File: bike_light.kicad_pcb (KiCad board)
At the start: 2 copper layers, 25.4 x 25.4 mm, 193 parts, among them Q1 AON7611, Q2 AON7611, Q3 AON7611, Q4 DMN65D8L, Q5 DMN65D8L, Q6 DMN65D8L, Q7 DMN65D8L, Q8 DMN65D8L, Q9 DMN65D8L, U1 TEST_PT, U10 TEST_PT, U11 TEST_PT, U12 TEST_PT, U13 TEST_PT, U14 TEST_PT, U15 TEST_PT, U16 TEST_PT, U17 TEST_PT, U18 TEST_PT, U19 TEST_PT, U2 TEST_PT, U20 MCP6L02, U21 74LVC2G06, U22 TPS3700, U23 NC7WZ08, U24 74LVC2G06, U25 TPS3700, U26 NC7WZ08, U27 74LVC2G06, U28 TPS3700, U29 NC7WZ08, U3 TEST_PT, U30 MSP430G2203IPW28, U31 BH1620FVC, U32 MMA7660FC, U33 AT42QT1011, U34 TOUCHPAD, U35 AT42QT1011, U36 TOUCHPAD, U37 AT42QT1011, U38 TOUCHPAD, U39 TLC59108IPWR, U4 TEST_PT, U40 TLC59108IPWR, U41 TLC59108IPWR, U42 TPS62090, U43 LM3668, U44 CONN_JTAG_14_2_wire, U45 CP2110, U46 ESDR0502N, U47 CONN_USB, U48 BQ24190, U5 TEST_PT, U6 TEST_PT, U7 TEST_PT, U8 TEST_PT, U9 TEST_PT

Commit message: Never thought 0805 would seem big...
But about 80% of the space is consumed by the 0805 resistor and caps.
01005? XD
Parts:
- C17, C18, C19, C20, C21, C22, C23, C24, C3, D14, D15, D16, D24, D25, D26, D27, D28, D29, D36, R31, R32, R33, R37, R38, R39, R40, R41, R42, R43, R44, U30, U39, U40, U41, U42: moved to B.Cu
- moved BT2 469.2 mm to (344.9, 191.5)
- moved D3 430.7 mm to (309.1, 132.8), turned to 45 degrees
- moved D4 424.1 mm to (310.5, 136.9), turned to 135 degrees
- moved R10 403.7 mm to (297.4, 131.2)
- moved R8 400.9 mm to (300.9, 144.8)
- moved U25 392.0 mm to (301.1, 142.1)
- moved U26 388.8 mm to (301.2, 136.8)
- moved R11 386.0 mm to (299.3, 129.0), turned to 180 degrees
- moved R9 382.8 mm to (304.8, 143.3)
- moved Q2 377.3 mm to (304.5, 135.5)
- moved R7 371.0 mm to (299.3, 133.3), turned to 180 degrees
- moved U24 362.8 mm to (301.8, 131.8)
- moved C21 339.3 mm to (355.9, 110.2)
- moved R42 333.3 mm to (349.4, 105.8), turned to 270 degrees
- moved C23 329.2 mm to (356.5, 105.8), turned to 270 degrees
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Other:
- board text added: "Rear Signal Module"
- board text removed: "Battery Control Module"

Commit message: moving around parts in pcb
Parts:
- moved D5 303.9 mm to (308.7, 131.1), turned to 45 degrees
- moved D6 296.4 mm to (309.8, 139.6), turned to 135 degrees
- moved R12 279.5 mm to (300.9, 124.1)
- moved Q3 277.6 mm to (309.0, 135.9)
- moved R15 274.0 mm to (301.6, 130.2)
- moved R13 268.1 mm to (302.1, 138.0)
- moved U28 266.0 mm to (305.2, 135.5)
- moved R16 254.4 mm to (300.7, 144.9)
- moved U27 247.5 mm to (301.4, 134.7)
- moved R14 239.9 mm to (299.5, 126.9)
- moved U29 235.6 mm to (301.8, 142.0), turned to 90 degrees
- moved BT3 235.4 mm to (231.0, 134.9)
- moved Q1 187.9 mm to (307.3, 77.0), turned to 180 degrees
- moved D2 165.1 mm to (308.6, 75.3), turned to 45 degrees
- moved D1 159.3 mm to (310.0, 82.8), turned to 135 degrees
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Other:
- board text added: "Front Signal Module"
- board text removed: "Rear Module"

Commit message: revisions to board and sch
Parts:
- removed BT2, BT3: BATTERY, BATT_18650
- removed D32: LY-E63F, LED_TOPLED_PWR
- removed D33, D34: LY-A67F, LED_SIDELED_PWR
- removed D35: LR-A67F, LED_SIDELED_PWR
- removed Q2, Q3: AON7611, DFN_3x3A_8L_EP1_P
- removed R13, R14: Nominal, r_0805
- removed R15: 102K, r_0805
- removed R16: 191K, r_0805
- removed R31, R32, R33, R34, R35, R36: 200, r_0805
- removed U24, U27: 74LVC2G06, SOT363
- removed U25, U28: TPS3700, SOT23_6_thin
- removed U26, U29: NC7WZ08, US8
- added P1: CONN_6_RA_MALE, CONN_3x2_MALE_RA, B.Cu at (461.0, 196.8)
- added P2: CONN_6_RA_FEMALE, CONN_3x2_FEMALE_RA, B.Cu at (335.3, 201.9)
- added P3: CONN_6_RA_MALE, CONN_3x2_MALE_RA, B.Cu at (344.2, 201.9)
- added P4: CONN_6_RA_MALE, CONN_3x2_MALE_RA, B.Cu at (313.7, 201.9)
- added P5: CONN_6_MALE_FRONT, CONN_3x2_FEMALE, B.Cu at (358.1, 201.9)
- added P6: CONN_6_MALE_BACK, CONN_3x2_FEMALE, B.Cu at (447.0, 196.8)
- BT1: moved to B.Cu
- D10: value LS-E63F -> LY-A67F; footprint LED_TOPLED_PWR -> LED_SIDELED_PWR; moved to B.Cu
- D11, D12, D13, D23: value LS-E63F -> LY-E63F
- D15, D16, D17, D18, D19: value LY-E63F -> LS-E63F
- D21, D22: value LS-E63F -> LR-A67F; footprint LED_TOPLED_PWR -> LED_SIDELED_PWR
- D26: value LY-E63F -> LY-A67F; footprint LED_TOPLED_PWR -> LED_SIDELED_PWR
- D28: value LY-A67F -> LY-E63F; footprint LED_SIDELED_PWR -> LED_TOPLED_PWR
- D29: value LR-A67F -> LY-E63F; footprint LED_SIDELED_PWR -> LED_TOPLED_PWR
- D3, D4, D5: value MBR1045ULPS -> LY-E63F; footprint TO_277B -> LED_TOPLED_PWR
- D6: value MBR1045ULPS -> LY-A67F; footprint TO_277B -> LED_SIDELED_PWR; moved to B.Cu
- R10: value 102K -> 200
- R11: value 191K -> 200
- R12, R7: value 1.58M -> 200
- R8, R9: value Nominal -> 200
- moved U20 550.8 mm to (388.6, 203.2)
- moved C2 549.8 mm to (387.4, 208.3)
- moved C1 543.4 mm to (387.4, 198.1)
- moved U11 513.3 mm to (401.3, 185.4)
- moved U14 513.3 mm to (381.0, 185.4)
- moved U17 513.3 mm to (426.7, 185.4)
- moved U18 513.3 mm to (419.1, 185.4)
- moved U2 513.3 mm to (388.6, 185.4)
- moved U3 513.3 mm to (439.4, 185.4)
- moved U6 513.3 mm to (408.9, 185.4)
- moved U8 513.3 mm to (368.3, 185.4)
- moved U1 513.3 mm to (386.1, 185.4)
- moved U10 513.3 mm to (398.8, 185.4)
- moved U12 513.3 mm to (393.7, 185.4)
- moved U13 513.3 mm to (406.4, 185.4)
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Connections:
- C22 pad 1: /output_signal_brake_2/+2.5V local -> /output_signal_brake_2/brake_leds/+2.5V
- D10 pad 1: /output_signal_brake_2/+2.5V local -> /output_signal_brake_2/brake_leds/+2.5V
- D10 pad 2: /output_signal_brake_2/+2.5V local -> /output_signal_brake_2/signal_leds_front/CATHODE_8
- D11 pad 1: /output_signal_brake_2/+2.5V local -> /output_signal_brake_2/brake_leds/+2.5V
- D11 pad 2: /output_signal_brake_2/+2.5V local -> /output_signal_brake_2/brake_leds/+2.5V
- D11 pad 3: /output_signal_brake_2/+2.5V local -> /output_signal_brake_2/brake_leds/+2.5V
- D11 pad 4: N-00000146 -> /output_signal_brake_2/signal_leds_front/CATHODE_1
- D12 pad 1: /output_signal_brake_2/+2.5V local -> /output_signal_brake_2/brake_leds/+2.5V
- D12 pad 2: /output_signal_brake_2/+2.5V local -> /output_signal_brake_2/brake_leds/+2.5V
- D12 pad 3: /output_signal_brake_2/+2.5V local -> /output_signal_brake_2/brake_leds/+2.5V
- D12 pad 4: N-00000167 -> /output_signal_brake_2/signal_leds_front/CATHODE_3
- D13 pad 1: /output_signal_brake_2/+2.5V local -> /output_signal_brake_2/brake_leds/+2.5V
- D13 pad 2: /output_signal_brake_2/+2.5V local -> /output_signal_brake_2/brake_leds/+2.5V
- D13 pad 3: /output_signal_brake_2/+2.5V local -> /output_signal_brake_2/brake_leds/+2.5V
- D13 pad 4: N-00000147 -> /output_signal_brake_2/signal_leds_front/CATHODE_5
- D14 pad 1: /output_signal_brake_2/+2.5V local -> /output_signal_brake_2/brake_leds/+2.5V
- D14 pad 2: /output_signal_brake_2/+2.5V local -> /output_signal_brake_2/brake_leds/+2.5V
- D14 pad 3: /output_signal_brake_2/+2.5V local -> /output_signal_brake_2/brake_leds/+2.5V
- D14 pad 4: N-00000112 (its old number) -> /output_signal_brake_2/signal_leds_front/CATHODE_7
- D15 pad 1: /output_signal_brake_2/+2.5V local -> /output_signal_brake_2/brake_leds/+2.5V
- D15 pad 2: /output_signal_brake_2/+2.5V local -> /output_signal_brake_2/brake_leds/+2.5V
- D15 pad 3: /output_signal_brake_2/+2.5V local -> /output_signal_brake_2/brake_leds/+2.5V
- D15 pad 4: N-00000113 -> /output_signal_brake_2/brake_leds/CATHODE_2
- D16 pad 1: /output_signal_brake_2/+2.5V local -> /output_signal_brake_2/brake_leds/+2.5V
- D16 pad 2: /output_signal_brake_2/+2.5V local -> /output_signal_brake_2/brake_leds/+2.5V
- D16 pad 3: /output_signal_brake_2/+2.5V local -> /output_signal_brake_2/brake_leds/+2.5V
- D16 pad 4: N-00000114 -> /output_signal_brake_2/brake_leds/CATHODE_4
- D17 pad 1: /output_signal_brake_2/+2.5V local -> /output_signal_brake_2/brake_leds/+2.5V
- D17 pad 2: /output_signal_brake_2/+2.5V local -> /output_signal_brake_2/brake_leds/+2.5V
- D17 pad 3: /output_signal_brake_2/+2.5V local -> /output_signal_brake_2/brake_leds/+2.5V
- D17 pad 4: N-00000140 -> /output_signal_brake_2/brake_leds/CATHODE_6
- D18 pad 1: /output_signal_brake_2/+2.5V local -> /output_signal_brake_2/brake_leds/+2.5V
- D18 pad 2: /output_signal_brake_2/+2.5V local -> /output_signal_brake_2/brake_leds/+2.5V
- D18 pad 3: /output_signal_brake_2/+2.5V local -> /output_signal_brake_2/brake_leds/+2.5V
- D18 pad 4: N-00000142 -> /output_signal_brake_2/brake_leds/CATHODE_1
- D19 pad 1: /output_signal_brake_2/+2.5V local -> /output_signal_brake_2/brake_leds/+2.5V
- D19 pad 2: /output_signal_brake_2/+2.5V local -> /output_signal_brake_2/brake_leds/+2.5V
- D19 pad 3: /output_signal_brake_2/+2.5V local -> /output_signal_brake_2/brake_leds/+2.5V
- D19 pad 4: N-00000164 (its old number) -> /output_signal_brake_2/brake_leds/CATHODE_3
- D20 pad 1: /output_signal_brake_2/+2.5V local -> /output_signal_brake_2/brake_leds/+2.5V
- D20 pad 2: /output_signal_brake_2/+2.5V local -> /output_signal_brake_2/brake_leds/+2.5V
- D20 pad 3: /output_signal_brake_2/+2.5V local -> /output_signal_brake_2/brake_leds/+2.5V
- D20 pad 4: N-00000168 -> /output_signal_brake_2/brake_leds/CATHODE_5
- D21 pad 1: /output_signal_brake_2/+2.5V local -> /output_signal_brake_2/brake_leds/+2.5V
- D21 pad 2: /output_signal_brake_2/+2.5V local -> /output_signal_brake_2/brake_leds/CATHODE_7
- D22 pad 1: /output_signal_brake_2/+2.5V local -> /output_signal_brake_2/brake_leds/+2.5V
- D22 pad 2: /output_signal_brake_2/+2.5V local -> /output_signal_brake_2/brake_leds/CATHODE_8
- D23 pad 1: /output_signal_brake_2/+2.5V local -> /output_signal_brake_2/brake_leds/+2.5V
- D23 pad 2: /output_signal_brake_2/+2.5V local -> /output_signal_brake_2/brake_leds/+2.5V
- D23 pad 3: /output_signal_brake_2/+2.5V local -> /output_signal_brake_2/brake_leds/+2.5V
- D23 pad 4: N-00000165 -> /output_signal_brake_2/signal_leds_back/CATHODE_2
- D24 pad 1: /output_signal_brake_2/+2.5V local -> /output_signal_brake_2/brake_leds/+2.5V
- D24 pad 2: /output_signal_brake_2/+2.5V local -> /output_signal_brake_2/brake_leds/+2.5V
- D24 pad 3: /output_signal_brake_2/+2.5V local -> /output_signal_brake_2/brake_leds/+2.5V
- D24 pad 4: N-00000109 -> /output_signal_brake_2/signal_leds_back/CATHODE_4
- D25 pad 1: /output_signal_brake_2/+2.5V local -> /output_signal_brake_2/brake_leds/+2.5V
- D25 pad 2: /output_signal_brake_2/+2.5V local -> /output_signal_brake_2/brake_leds/+2.5V
- D25 pad 3: /output_signal_brake_2/+2.5V local -> /output_signal_brake_2/brake_leds/+2.5V
- D25 pad 4: N-00000110 (its old number) -> /output_signal_brake_2/signal_leds_back/CATHODE_6
- D26 pad 1: /output_signal_brake_2/+2.5V local -> /output_signal_brake_2/brake_leds/+2.5V
- D26 pad 2: /output_signal_brake_2/+2.5V local -> /output_signal_brake_2/signal_leds_back/CATHODE_8
- D27 pad 1: /output_signal_brake_2/+2.5V local -> /output_signal_brake_2/brake_leds/+2.5V
- D27 pad 2: N-00000170 -> /output_signal_brake_2/signal_leds_back/CATHODE_8
- D28 pad 1: /output_signal_brake_2/+2.5V local -> /output_signal_brake_2/brake_leds/+2.5V
- D28 pad 2: N-00000170 -> /output_signal_brake_2/brake_leds/+2.5V
- D29 pad 1: /output_signal_brake_2/+2.5V local -> /output_signal_brake_2/brake_leds/+2.5V
- D29 pad 2: N-00000169 -> /output_signal_brake_2/brake_leds/+2.5V
- D3 pad 1: N-00000193 -> /output_signal_brake_2/brake_leds/+2.5V
- D3 pad 2: N-00000193 -> /output_signal_brake_2/brake_leds/+2.5V
- D3 pad 3: N-00000198 -> /output_signal_brake_2/brake_leds/+2.5V
- D30 pad 1: /output_signal_brake_2/+2.5V local -> /output_signal_brake_2/brake_leds/+2.5V
- D30 pad 2: /output_signal_brake_2/+2.5V local -> /output_signal_brake_2/brake_leds/+2.5V
- D30 pad 3: /output_signal_brake_2/+2.5V local -> /output_signal_brake_2/brake_leds/+2.5V
- D30 pad 4: N-00000144 -> /output_signal_brake_2/signal_leds_back/CATHODE_5
- D31 pad 1: /output_signal_brake_2/+2.5V local -> /output_signal_brake_2/brake_leds/+2.5V
- D31 pad 2: /output_signal_brake_2/+2.5V local -> /output_signal_brake_2/brake_leds/+2.5V
- D31 pad 3: /output_signal_brake_2/+2.5V local -> /output_signal_brake_2/brake_leds/+2.5V
- D31 pad 4: N-00000141 -> /output_signal_brake_2/signal_leds_back/CATHODE_7
- D4 pad 1: N-00000199 -> /output_signal_brake_2/brake_leds/+2.5V
- D4 pad 2: N-00000199 -> /output_signal_brake_2/brake_leds/+2.5V
- D4 pad 3: N-00000193 -> /output_signal_brake_2/brake_leds/+2.5V
- D5 pad 1: N-00000212 -> /output_signal_brake_2/brake_leds/+2.5V
- D5 pad 2: N-00000212 -> /output_signal_brake_2/brake_leds/+2.5V
- D5 pad 3: N-00000208 -> /output_signal_brake_2/brake_leds/+2.5V
- D6 pad 1: N-00000211 -> /output_signal_brake_2/brake_leds/+2.5V
- D6 pad 2: N-00000211 -> /output_signal_brake_2/signal_leds_front/CATHODE_8
- R10 pad 1: N-00000200 -> /output_signal_brake_2/brake_leds/+2.5V
- R10 pad 2: N-00000202 -> /output_signal_brake_2/brake_leds/CATHODE_8
- R11 pad 1: N-00000202 -> /output_signal_brake_2/brake_leds/+2.5V
- R11 pad 2: AGND -> /output_signal_brake_2/brake_leds/CATHODE_8
- R12 pad 1: N-00000212 -> /output_signal_brake_2/brake_leds/+2.5V
- R12 pad 2: N-00000205 -> /output_signal_brake_2/signal_leds_back/CATHODE_8
- R42 pad 1: /output_signal_brake_2/+2.5V local -> /output_signal_brake_2/brake_leds/+2.5V
- R43 pad 1: /output_signal_brake_2/+2.5V local -> /output_signal_brake_2/brake_leds/+2.5V
- R7 pad 1: N-00000193 -> /output_signal_brake_2/brake_leds/+2.5V
- R7 pad 2: N-00000200 -> /output_signal_brake_2/signal_leds_front/CATHODE_8
- R8 pad 1: +3.3V -> /output_signal_brake_2/brake_leds/+2.5V
- R8 pad 2: /battery_pack/battery_module_2/~UV -> /output_signal_brake_2/brake_leds/CATHODE_7
- R9 pad 1: +3.3V -> /output_signal_brake_2/brake_leds/+2.5V
- R9 pad 2: /battery_pack/battery_module_2/~OV -> /output_signal_brake_2/brake_leds/CATHODE_7
- U39 pad 10: N-00000146 -> /output_signal_brake_2/signal_leds_front/CATHODE_4
- U39 pad 11: N-00000148 -> /output_signal_brake_2/signal_leds_front/CATHODE_5
- U39 pad 12: N-00000167 -> /output_signal_brake_2/signal_leds_front/CATHODE_6
- U39 pad 14: N-00000165 -> /output_signal_brake_2/signal_leds_front/CATHODE_7
- U39 pad 15: N-00000147 -> /output_signal_brake_2/signal_leds_front/CATHODE_8
- U39 pad 6: N-00000168 -> /output_signal_brake_2/signal_leds_front/CATHODE_1
- U39 pad 7: N-00000145 -> /output_signal_brake_2/signal_leds_front/CATHODE_2
- U39 pad 9: N-00000166 -> /output_signal_brake_2/signal_leds_front/CATHODE_3
- U40 pad 10: N-00000113 -> /output_signal_brake_2/signal_leds_back/CATHODE_4
- U40 pad 11: N-00000111 -> /output_signal_brake_2/signal_leds_back/CATHODE_5
- U40 pad 12: N-00000114 -> /output_signal_brake_2/signal_leds_back/CATHODE_6
- U40 pad 14: N-00000170 -> /output_signal_brake_2/signal_leds_back/CATHODE_7
- U40 pad 15: N-00000169 -> /output_signal_brake_2/signal_leds_back/CATHODE_8
- U40 pad 6: N-00000109 -> /output_signal_brake_2/signal_leds_back/CATHODE_1
- U40 pad 7: N-00000112 (its old number) -> /output_signal_brake_2/signal_leds_back/CATHODE_2
- U40 pad 9: N-00000110 (its old number) -> /output_signal_brake_2/signal_leds_back/CATHODE_3
- U41 pad 10: N-00000142 -> /output_signal_brake_2/brake_leds/CATHODE_4
- U41 pad 11: N-00000143 -> /output_signal_brake_2/brake_leds/CATHODE_5
- U41 pad 12: N-00000164 (its old number) -> /output_signal_brake_2/brake_leds/CATHODE_6
- U41 pad 14: N-00000163 (its old number) -> /output_signal_brake_2/brake_leds/CATHODE_7
- U41 pad 15: N-00000139 -> /output_signal_brake_2/brake_leds/CATHODE_8
- U41 pad 6: N-00000144 -> /output_signal_brake_2/brake_leds/CATHODE_1
- U41 pad 7: N-00000140 -> /output_signal_brake_2/brake_leds/CATHODE_2
- U41 pad 9: N-00000141 -> /output_signal_brake_2/brake_leds/CATHODE_3
- U42 pad 16: /output_signal_brake_2/+2.5V local -> /output_signal_brake_2/brake_leds/+2.5V
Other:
- board outline removed

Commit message: revised layout considerably. more compact
almost ready for routing
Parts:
- C20, C21, C22, C23, C24, C3, D15, D16, D24, D25, D28, D29, D36, R40, R41, R42, R43, R44, U30, U42: moved to F.Cu
- D21, D22, D31, R10, R11, R12, R7, R8, R9: moved to B.Cu
- moved R7 188.5 mm to (468.6, 194.3)
- moved C29 174.6 mm to (432.6, 193.8)
- moved R46 173.1 mm to (432.6, 196.1)
- moved U44 172.3 mm to (411.0, 193.5)
- moved U40 170.2 mm to (306.1, 199.4)
- moved C17 168.0 mm to (306.1, 205.7), turned to 180 degrees
- moved R38 167.7 mm to (306.1, 208.3), turned to 180 degrees
- moved R47 162.4 mm to (396.0, 197.1)
- moved C30 158.3 mm to (396.5, 194.8)
- moved R37 157.5 mm to (468.6, 205.7)
- moved U45 157.1 mm to (401.1, 200.2), turned to 270 degrees
- moved C27 156.8 mm to (432.6, 189.2)
- moved C28 154.3 mm to (432.6, 191.5)
- moved U46 154.1 mm to (401.1, 195.8), turned to 90 degrees
- moved C19 153.2 mm to (466.1, 205.7)
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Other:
- board text added: "Back Signal"
- board text added: "Brake"
- board text added: "Touch Adj +"
- board text added: "Touch Adj -"
- board text added: "Touch Main"
- board text removed: "Battery Module"
- board text removed: "Battery modules"
- board text removed: "Front Signal Module"
- board text removed: "Interaction Module"
- board text removed: "Interface Module"
- board text removed: "Rear Signal Module"
- board text removed: "Sensor Module"

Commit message: replacement of parts, moved parts, preparing for routing
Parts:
- added L1: 1uH, smt_1816, F.Cu at (388.5, 189.4)
- added L2: 2.2uH, smt_1008, F.Cu at (400.8, 205.7)
- added L3: 2.2uH, smt_1816, F.Cu at (389.9, 198.5)
- added R1: R, r_0805, F.Cu at (386.3, 209.8)
- added TH1: NTC 10K, r_0402, F.Cu at (367.4, 201.8)
- added TH2: NTC 10K, r_0402, F.Cu at (376.9, 196.1)
- C1, C10, C11, C12, C13, C14, C15, C16, C17, C18, C19, C2, C20, C21, C22, C23, C24, C25, C26, C27, C28, C29, C3, C30, C31, C32, C33, C34, C35, C36, C37, C4, C5, C6, C7, C8, C9, R10, R11, R12, R17, R18, R19, R2, R20, R21, R22, R23, R24, R25, R26, R27, R28, R29, R3, R30, R37, R38, R39, R4, R40, R41, R42, R43, R44, R45, R46, R47, R48, R49, R5, R50, R51, R52, R53, R54, R55, R56, R57, R58, R6, R7, R8, R9: footprint r_0805 -> r_0603
- P1, P3, P4: footprint CONN_3x2_MALE_RA -> CONN_6_MALE_RA
- P2: footprint CONN_3x2_FEMALE_RA -> CONN_6_FEMALE
- P5, P6: footprint CONN_3x2_FEMALE -> CONN_6_FEMALE
- U43: footprint bnc -> WSON_12
- moved U43 74.0 mm to (404.5, 206.8), turned to 270 degrees
- moved R57 27.7 mm to (367.0, 203.2)
- moved U23 19.6 mm to (374.3, 189.6), turned to 180 degrees
- moved U21 17.7 mm to (376.4, 190.9), turned to 180 degrees
- moved R7 16.6 mm to (461.0, 209.0), turned to 90 degrees
- moved Q1 15.4 mm to (369.6, 192.5), turned to 0 degrees
- moved R58 14.9 mm to (377.1, 197.6)
- moved R6 14.0 mm to (361.9, 203.2), turned to 270 degrees
- moved U48 13.7 mm to (395.4, 195.8), turned to 90 degrees
- moved R40 13.5 mm to (360.2, 195.7), turned to 180 degrees
- moved C20 12.5 mm to (360.2, 197.4), turned to 180 degrees
- moved C3 12.3 mm to (426.0, 209.6), turned to 180 degrees
- moved R5 12.2 mm to (361.9, 200.4), turned to 270 degrees
- moved R37 11.9 mm to (463.8, 194.8), turned to 0 degrees
- moved D1 11.6 mm to (361.9, 194.1)
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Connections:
- R41 pad 1: (no net) -> /output_signal_brake_2/brake_leds/+2.5V
- R41 pad 2: (no net) -> N-00000163
- R44 pad 1: (no net) -> N-00000163
- R44 pad 2: (no net) -> AGND

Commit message: organizing parts...
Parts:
- moved L2 293.4 mm to (146.2, 60.1)
- moved R45 293.1 mm to (153.3, 63.4)
- moved C25 293.1 mm to (147.1, 63.8)
- moved D37 293.1 mm to (150.7, 64.0)
- moved U43 293.1 mm to (150.0, 61.3)
- moved C26 293.0 mm to (153.3, 60.6)
- moved R1 290.7 mm to (127.1, 78.1)
- moved U48 286.5 mm to (134.1, 78.1), turned to 135 degrees
- moved R54 283.5 mm to (134.1, 74.3), turned to 90 degrees
- moved U20 281.5 mm to (127.5, 74.0), turned to 90 degrees
- moved L3 281.2 mm to (133.1, 83.8), turned to 180 degrees
- moved C21 280.7 mm to (137.4, 66.5)
- moved C22 280.7 mm to (135.8, 61.1)
- moved C23 280.7 mm to (131.3, 63.8)
- moved C24 280.7 mm to (132.6, 66.7)
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
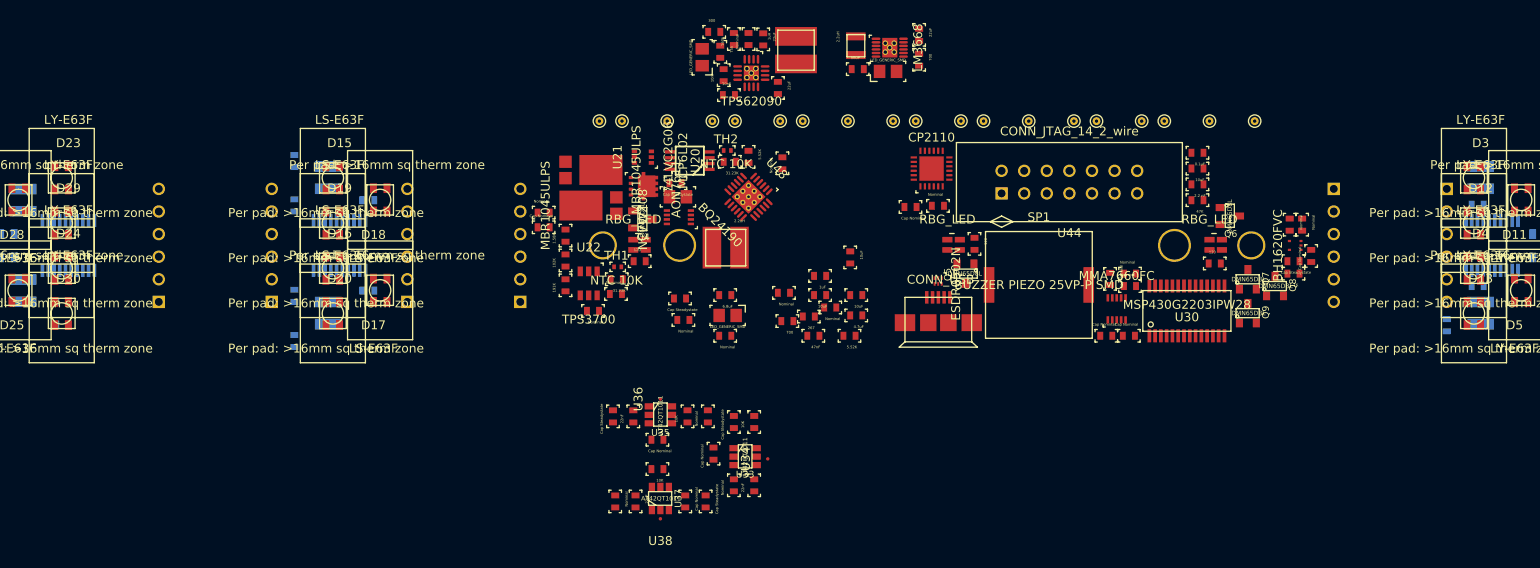
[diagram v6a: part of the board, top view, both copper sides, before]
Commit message: rearranged components, revised footprints
also planned power/gnd planes. haven't routed anything yet
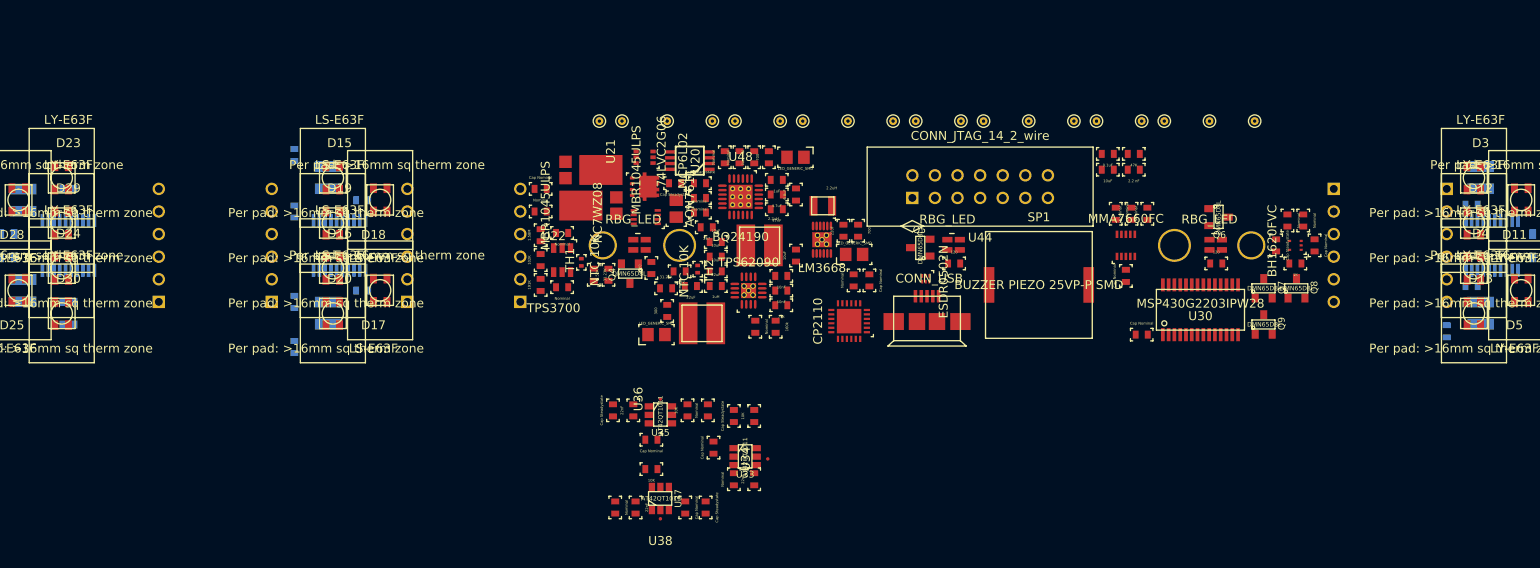
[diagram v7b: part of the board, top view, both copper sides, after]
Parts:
- moved L1 33.5 mm to (130.4, 92.3), turned to 180 degrees
- moved R41 33.4 mm to (137.2, 92.7), turned to 90 degrees
- moved R43 33.0 mm to (134.9, 92.7), turned to 90 degrees
- moved D36 32.4 mm to (124.7, 93.6), turned to 180 degrees
- moved R42 31.9 mm to (125.0, 90.9), turned to 270 degrees
- moved R44 28.6 mm to (137.8, 90.3), turned to 0 degrees
- moved C22 28.2 mm to (127.6, 88.1), turned to 0 degrees
- moved R53 27.3 mm to (118.4, 86.9), turned to 270 degrees
- moved C23 25.7 mm to (137.8, 88.6), turned to 0 degrees
- moved U42 24.4 mm to (134.1, 88.6), turned to 0 degrees
- moved C26 23.0 mm to (144.8, 81.9), turned to 270 degrees
- moved U43 22.9 mm to (142.4, 82.9), turned to 180 degrees
- moved C21 22.7 mm to (130.4, 88.1), turned to 180 degrees
- moved C25 22.3 mm to (139.4, 84.7), turned to 270 degrees
- moved C24 21.0 mm to (137.8, 87.0), turned to 0 degrees
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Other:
- board text added: "Front"

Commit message: parts arranged plausibly
maybe ready for routing?
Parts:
- moved P2 88.9 mm to (157.9, 46.1)
- moved P4 88.7 mm to (144.8, 45.8)
- moved R38 27.9 mm to (82.0, 79.0), turned to 0 degrees
- moved U40 26.3 mm to (83.9, 83.6)
- moved D26 25.9 mm to (78.5, 87.4)
- moved D27 25.9 mm to (78.5, 79.6)
- moved D25 25.6 mm to (76.8, 88.1)
- moved D28 25.5 mm to (76.8, 79.0)
- moved C17 24.4 mm to (82.0, 88.3), turned to 0 degrees
- moved D31 24.0 mm to (74.0, 83.6)
- moved D23 23.1 mm to (80.6, 76.7)
- moved D29 23.0 mm to (80.6, 81.3)
- moved D24 23.0 mm to (80.6, 85.9)
- moved D30 23.0 mm to (80.6, 90.4)
- moved R12 21.8 mm to (78.5, 83.6), turned to 90 degrees
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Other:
- board text added: "18650"
- board text added: "26650"
